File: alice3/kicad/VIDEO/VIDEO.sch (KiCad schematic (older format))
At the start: 4 parts, among them SW1 SW_PUSH, U1 Propeller_P8X32A-D40, Y1 5 MHz

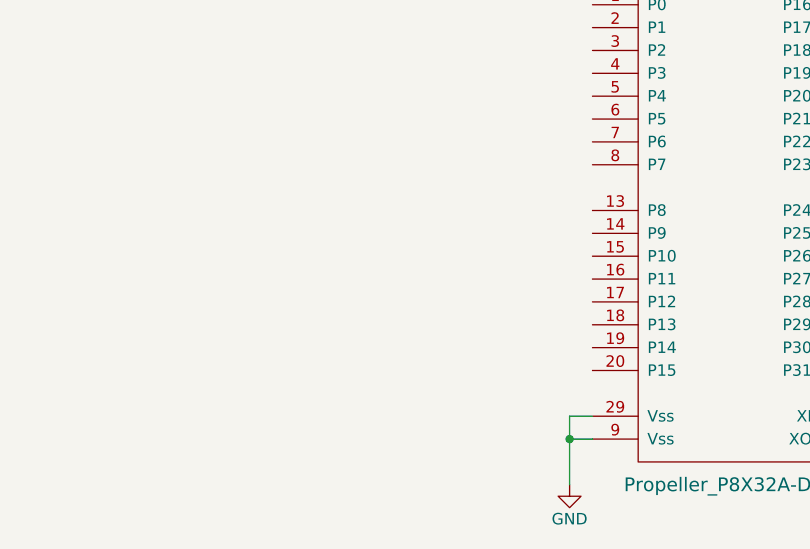
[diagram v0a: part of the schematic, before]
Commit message: Add VGA daughter board.
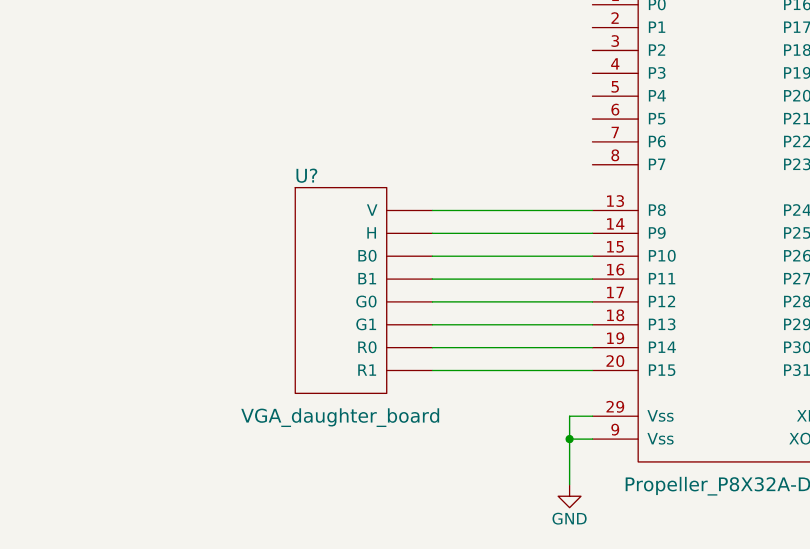
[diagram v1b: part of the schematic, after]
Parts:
- added U?: VGA_daughter_board, symbol VGA_daughter_board
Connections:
- net at U1.13 (P8): now also U?.~ (V)
- net at U1.14 (P9): now also U?.~ (V)
- net at U1.15 (P10): now also U?.~ (V)
- net at U1.16 (P11): now also U?.~ (V)
- net at U1.17 (P12): now also U?.~ (V)
- net at U1.18 (P13): now also U?.~ (V)
- net at U1.19 (P14): now also U?.~ (V)
- net at U1.20 (P15): now also U?.~ (V)
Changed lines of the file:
@@
 LIBS:valves
 LIBS:propeller_p8x32a-d40
+LIBS:vga_daughter_board
 LIBS:VIDEO-cache
 EELAYER 25 0
@@
 Wire Wire Line
 	1000 1200 1000 1500
+$Comp
+L VGA_daughter_board U?
+U 1 1 5681E1A9
+P 3800 3950
+F 0 "U?" H 3550 4450 60  0000 C CNN
+F 1 "VGA_daughter_board" H 3700 3400 60  0000 C CNN
+F 2 "" H 3800 4000 60  0000 C CNN
+F 3 "" H 3800 4000 60  0000 C CNN
+	1    3800 3950
+	1    0    0    -1
+$EndComp
+Wire Wire Line
+	4100 3600 4800 3600
+Wire Wire Line
+	4100 3700 4800 3700
+Wire Wire Line
+	4100 3800 4800 3800
+Wire Wire Line
+	4100 3900 4800 3900
+Wire Wire Line
+	4100 4000 4800 4000
+Wire Wire Line
+	4100 4100 4800 4100
+Wire Wire Line
+	4100 4200 4800 4200
+Wire Wire Line
+	4100 4300 4800 4300
 $EndSCHEMATC

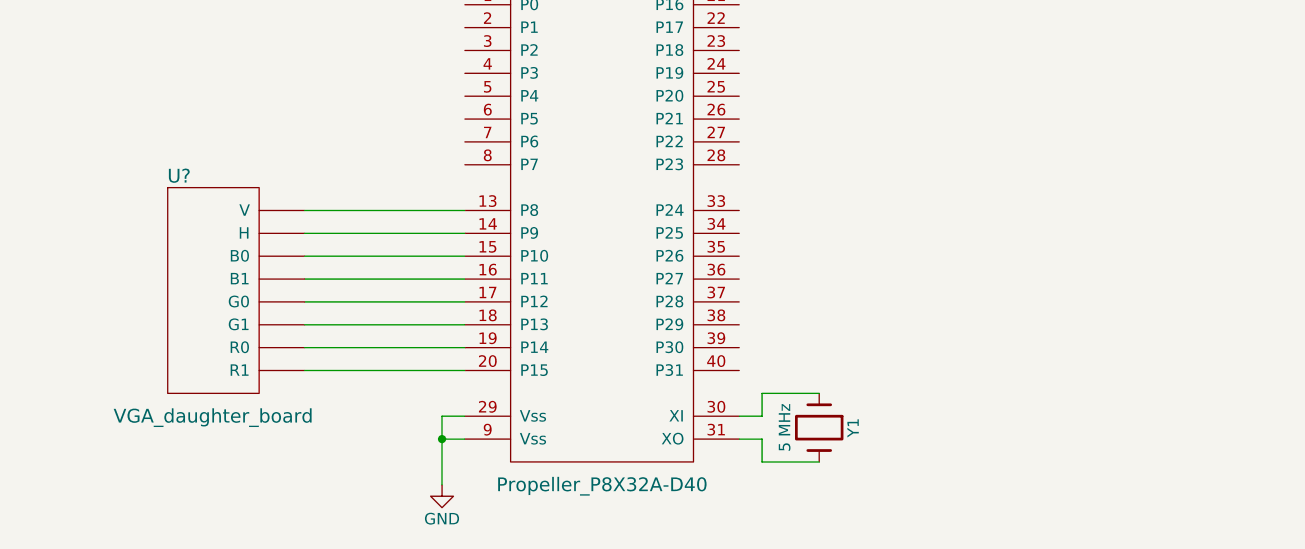
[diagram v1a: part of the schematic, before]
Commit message: Add 24LC256 EEPROM chip to VIDEO board.
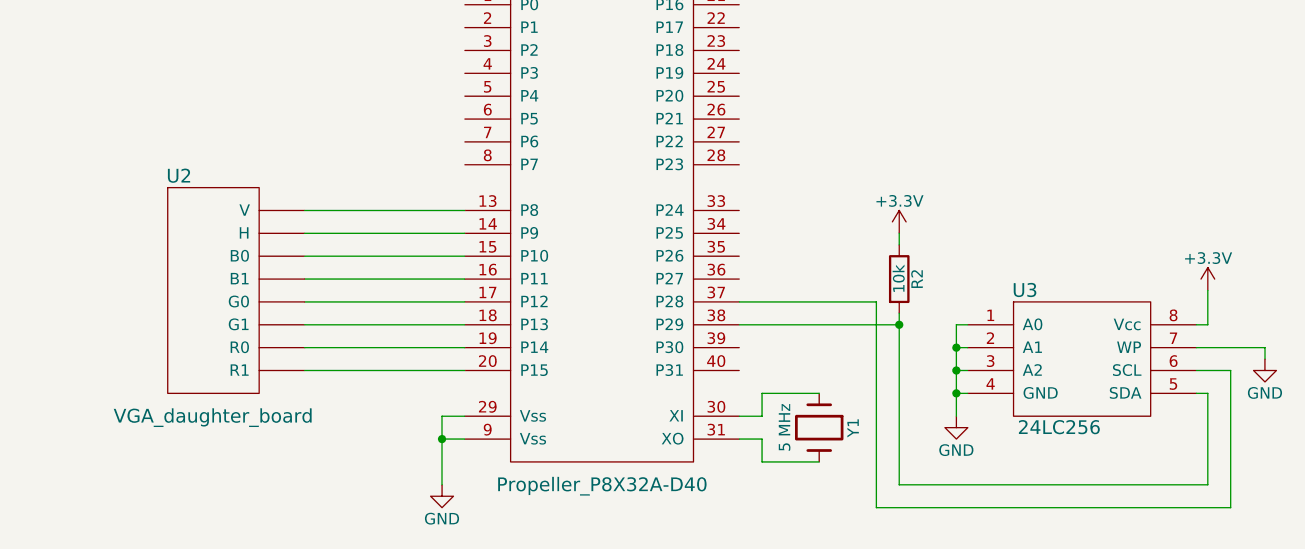
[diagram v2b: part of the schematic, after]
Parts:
- added R2: 10k, symbol R
- added U3: 24LC256, symbol 24LC256
- gave numbers to parts that had none: 1
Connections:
- net +3V3: now also R2.1, U3.8 (Vcc)
- net GND: now also U3.1 (A0), U3.2 (A1), U3.3 (A2), U3.4 (GND), U3.7 (WP)
- net at U1.37 (P28): now also U3.6 (SCL)
- net at U1.38 (P29): now also R2.2, U3.5 (SDA)
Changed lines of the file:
@@
 LIBS:propeller_p8x32a-d40
 LIBS:vga_daughter_board
+LIBS:24lc256
 LIBS:VIDEO-cache
 EELAYER 25 0
@@
 $EndComp
 $Comp
-L GND #PWR01
+L GND #PWR4
 U 1 1 566E4A0D
 P 4700 4800
-F 0 "#PWR01" H 4700 4550 50  0001 C CNN
+F 0 "#PWR4" H 4700 4550 50  0001 C CNN
 F 1 "GND" H 4700 4650 50  0000 C CNN
 F 2 "" H 4700 4800 50  0000 C CNN
@@
 Connection ~ 4700 4600
 $Comp
-L +3.3V #PWR02
+L +3.3V #PWR3
 U 1 1 566E4A37
 P 4700 2200
-F 0 "#PWR02" H 4700 2050 50  0001 C CNN
+F 0 "#PWR3" H 4700 2050 50  0001 C CNN
 F 1 "+3.3V" H 4700 2340 50  0000 C CNN
 F 2 "" H 4700 2200 50  0000 C CNN
@@
 	6100 4700 6350 4700
 $Comp
-L GND #PWR03
+L GND #PWR5
 U 1 1 566E4B37
 P 6300 2500
-F 0 "#PWR03" H 6300 2250 50  0001 C CNN
+F 0 "#PWR5" H 6300 2250 50  0001 C CNN
 F 1 "GND" H 6300 2350 50  0000 C CNN
 F 2 "" H 6300 2500 50  0000 C CNN
@@
 	6000 2500 6300 2500
 $Comp
-L +3.3V #PWR04
+L +3.3V #PWR6
 U 1 1 566E4B67
 P 6500 1800
-F 0 "#PWR04" H 6500 1650 50  0001 C CNN
+F 0 "#PWR6" H 6500 1650 50  0001 C CNN
 F 1 "+3.3V" H 6500 1940 50  0000 C CNN
 F 2 "" H 6500 1800 50  0000 C CNN
@@
 $EndComp
 $Comp
-L GND #PWR05
+L GND #PWR9
 U 1 1 566E4C07
 P 7200 2500
-F 0 "#PWR05" H 7200 2250 50  0001 C CNN
+F 0 "#PWR9" H 7200 2250 50  0001 C CNN
 F 1 "GND" H 7200 2350 50  0000 C CNN
 F 2 "" H 7200 2500 50  0000 C CNN
@@
 	7200 2400 7200 2500
 $Comp
-L PWR_FLAG #FLG06
+L PWR_FLAG #FLG1
 U 1 1 566E4C94
 P 1000 1200
-F 0 "#FLG06" H 1000 1295 50  0001 C CNN
+F 0 "#FLG1" H 1000 1295 50  0001 C CNN
 F 1 "PWR_FLAG" H 1000 1380 50  0000 C CNN
 F 2 "" H 1000 1200 50  0000 C CNN
@@
 $EndComp
 $Comp
-L PWR_FLAG #FLG07
+L PWR_FLAG #FLG2
 U 1 1 566E4CCE
 P 1500 1200
-F 0 "#FLG07" H 1500 1295 50  0001 C CNN
+F 0 "#FLG2" H 1500 1295 50  0001 C CNN
 F 1 "PWR_FLAG" H 1500 1380 50  0000 C CNN
 F 2 "" H 1500 1200 50  0000 C CNN
@@
 $EndComp
 $Comp
-L +3.3V #PWR08
+L +3.3V #PWR1
 U 1 1 566E4D29
 P 1000 1500
-F 0 "#PWR08" H 1000 1350 50  0001 C CNN
+F 0 "#PWR1" H 1000 1350 50  0001 C CNN
 F 1 "+3.3V" H 1000 1640 50  0000 C CNN
 F 2 "" H 1000 1500 50  0000 C CNN
@@
 $EndComp
 $Comp
-L GND #PWR09
+L GND #PWR2
 U 1 1 566E4D40
 P 1500 1500
-F 0 "#PWR09" H 1500 1250 50  0001 C CNN
+F 0 "#PWR2" H 1500 1250 50  0001 C CNN
 F 1 "GND" H 1500 1350 50  0000 C CNN
 F 2 "" H 1500 1500 50  0000 C CNN
@@
 	1000 1200 1000 1500
 $Comp
-L VGA_daughter_board U?
+L VGA_daughter_board U2
 U 1 1 5681E1A9
 P 3800 3950
-F 0 "U?" H 3550 4450 60  0000 C CNN
+F 0 "U2" H 3550 4450 60  0000 C CNN
 F 1 "VGA_daughter_board" H 3700 3400 60  0000 C CNN
 F 2 "" H 3800 4000 60  0000 C CNN
@@
 Wire Wire Line
 	4100 4300 4800 4300
+$Comp
+L 24LC256 U3
+U 1 1 5681F117
+P 7500 4250
+F 0 "U3" H 7250 4550 60  0000 C CNN
+F 1 "24LC256" H 7400 3950 60  0000 C CNN
+F 2 "" H 7500 4150 60  0000 C CNN
+F 3 "" H 7500 4150 60  0000 C CNN
+	1    7500 4250
+	1    0    0    -1
+$EndComp
+$Comp
+L GND #PWR8
+U 1 1 5681F164
+P 6950 4500
+F 0 "#PWR8" H 6950 4250 50  0001 C CNN
+F 1 "GND" H 6950 4350 50  0000 C CNN
+F 2 "" H 6950 4500 50  0000 C CNN
+F 3 "" H 6950 4500 50  0000 C CNN
+	1    6950 4500
+	1    0    0    -1
+$EndComp
+Wire Wire Line
+	7000 4100 6950 4100
+Wire Wire Line
+	6950 4100 6950 4500
+Wire Wire Line
+	7000 4200 6950 4200
+Connection ~ 6950 4200
+Wire Wire Line
+	7000 4300 6950 4300
+Connection ~ 6950 4300
+Wire Wire Line
+	7000 4400 6950 4400
+Connection ~ 6950 4400
+$Comp
+L +3.3V #PWR10
+U 1 1 5681F2C2
+P 8050 3950
+F 0 "#PWR10" H 8050 3800 50  0001 C CNN
+F 1 "+3.3V" H 8050 4090 50  0000 C CNN
+F 2 "" H 8050 3950 50  0000 C CNN
+F 3 "" H 8050 3950 50  0000 C CNN
+	1    8050 3950
+	1    0    0    -1
+$EndComp
+$Comp
+L GND #PWR11
+U 1 1 5681F2E8
+P 8300 4250
+F 0 "#PWR11" H 8300 4000 50  0001 C CNN
+F 1 "GND" H 8300 4100 50  0000 C CNN
+F 2 "" H 8300 4250 50  0000 C CNN
+F 3 "" H 8300 4250 50  0000 C CNN
+	1    8300 4250
+	1    0    0    -1
+$EndComp
+Wire Wire Line
+	8000 4100 8050 4100
+Wire Wire Line
+	8050 4100 8050 3950
+Wire Wire Line
+	8000 4200 8300 4200
+Wire Wire Line
+	8300 4200 8300 4250
+Wire Wire Line
+	8000 4300 8150 4300
+Wire Wire Line
+	8150 4300 8150 4900
+Wire Wire Line
+	8150 4900 6600 4900
+Wire Wire Line
+	6600 4900 6600 4000
+Wire Wire Line
+	6600 4000 6000 4000
+Wire Wire Line
+	8000 4400 8050 4400
+Wire Wire Line
+	8050 4400 8050 4800
+Wire Wire Line
+	8050 4800 6700 4800
+Wire Wire Line
+	6700 4800 6700 4050
+Wire Wire Line
+	6700 4100 6000 4100
+$Comp
+L +3.3V #PWR7
+U 1 1 5681F435
+P 6700 3700
+F 0 "#PWR7" H 6700 3550 50  0001 C CNN
+F 1 "+3.3V" H 6700 3840 50  0000 C CNN
+F 2 "" H 6700 3700 50  0000 C CNN
+F 3 "" H 6700 3700 50  0000 C CNN
+	1    6700 3700
+	1    0    0    -1
+$EndComp
+$Comp
+L R R2
+U 1 1 5681F454
+P 6700 3900
+F 0 "R2" V 6780 3900 50  0000 C CNN
+F 1 "10k" V 6700 3900 50  0000 C CNN
+F 2 "" V 6630 3900 50  0000 C CNN
+F 3 "" H 6700 3900 50  0000 C CNN
+	1    6700 3900
+	1    0    0    -1
+$EndComp
+Connection ~ 6700 4100
+Wire Wire Line
+	6700 3750 6700 3700
 $EndSCHEMATC

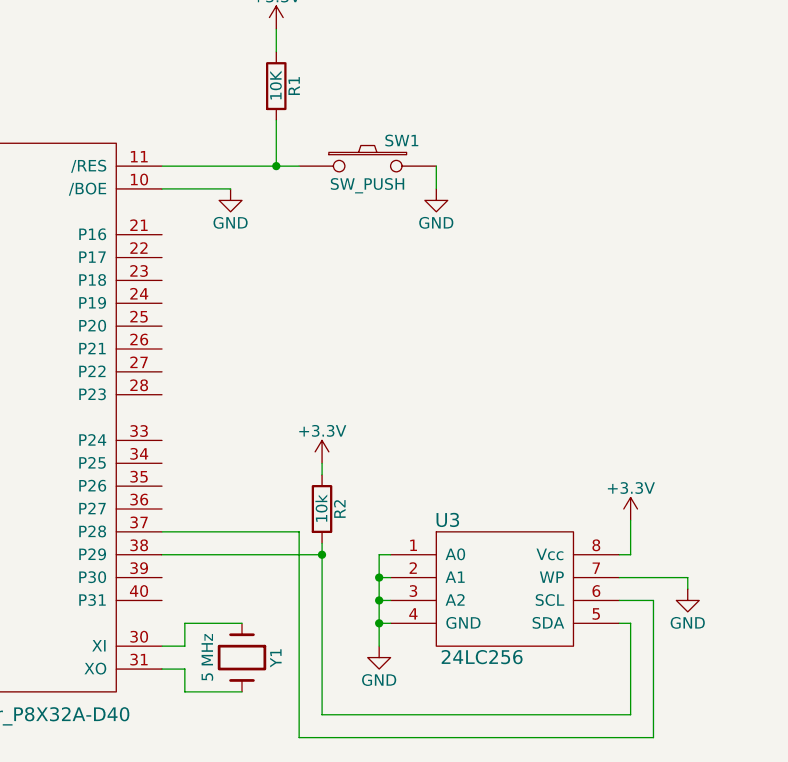
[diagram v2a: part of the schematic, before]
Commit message: Add Propeller Plug (USB programmer).
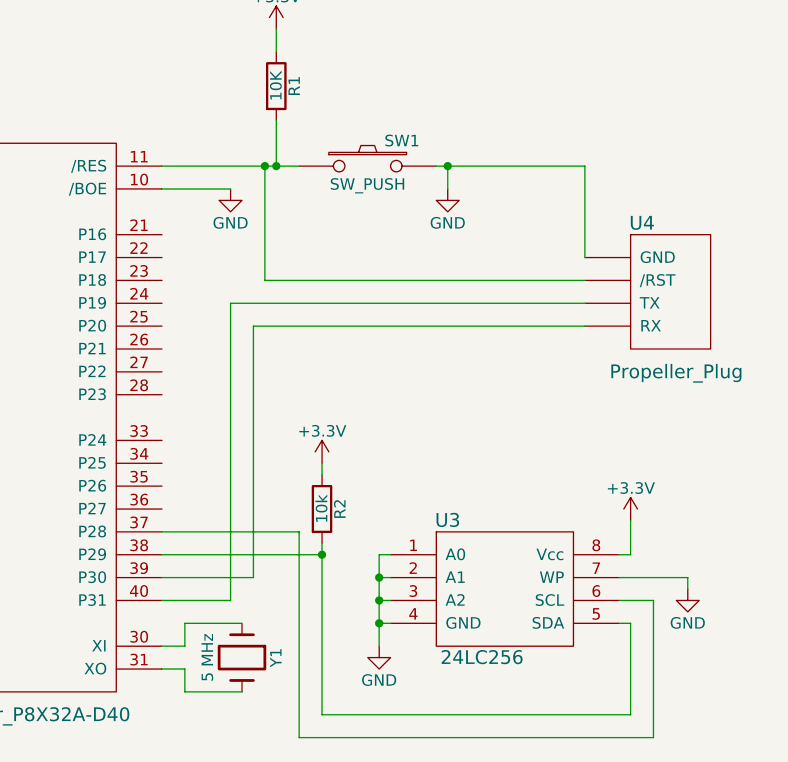
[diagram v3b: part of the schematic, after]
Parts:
- added U4: Propeller_Plug, symbol Propeller_Plug
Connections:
- net GND: now also U4.~ (TX)
- net at R1.2, SW1.1, U1.11 (/RES): now also U4.~ (TX)
- net at U1.39 (P30): now also U4.~ (TX)
- net at U1.40 (P31): now also U4.~ (TX)
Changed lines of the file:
@@
 LIBS:vga_daughter_board
 LIBS:24lc256
+LIBS:propeller_plug
 LIBS:VIDEO-cache
 EELAYER 25 0
@@
 	1    0    0    -1
 $EndComp
-Wire Wire Line
-	4800 4500 4700 4500
-Wire Wire Line
-	4700 4500 4700 4800
-Wire Wire Line
-	4800 4600 4700 4600
-Connection ~ 4700 4600
 $Comp
 L +3.3V #PWR3
@@
 	1    0    0    -1
 $EndComp
-Wire Wire Line
-	4700 2500 4800 2500
-Wire Wire Line
-	4700 2200 4700 2500
-Wire Wire Line
-	4800 2400 4700 2400
-Connection ~ 4700 2400
 $Comp
 L Crystal Y1
@@
 	0    1    1    0
 $EndComp
-Wire Wire Line
-	6000 4500 6100 4500
-Wire Wire Line
-	6100 4500 6100 4400
-Wire Wire Line
-	6100 4400 6350 4400
-Wire Wire Line
-	6000 4600 6100 4600
-Wire Wire Line
-	6100 4600 6100 4700
-Wire Wire Line
-	6100 4700 6350 4700
 $Comp
 L GND #PWR5
@@
 	1    0    0    -1
 $EndComp
-Wire Wire Line
-	6000 2500 6300 2500
 $Comp
 L +3.3V #PWR6
@@
 L GND #PWR9
 U 1 1 566E4C07
-P 7200 2500
-F 0 "#PWR9" H 7200 2250 50  0001 C CNN
-F 1 "GND" H 7200 2350 50  0000 C CNN
-F 2 "" H 7200 2500 50  0000 C CNN
-F 3 "" H 7200 2500 50  0000 C CNN
-	1    7200 2500
-	1    0    0    -1
-$EndComp
-Wire Wire Line
-	6500 1900 6500 1800
-Wire Wire Line
-	6000 2400 6600 2400
-Wire Wire Line
-	6500 2400 6500 2200
-Connection ~ 6500 2400
-Wire Wire Line
-	7200 2400 7200 2500
+P 7250 2500
+F 0 "#PWR9" H 7250 2250 50  0001 C CNN
+F 1 "GND" H 7250 2350 50  0000 C CNN
+F 2 "" H 7250 2500 50  0000 C CNN
+F 3 "" H 7250 2500 50  0000 C CNN
+	1    7250 2500
+	1    0    0    -1
+$EndComp
 $Comp
 L PWR_FLAG #FLG1
@@
 	1    0    0    -1
 $EndComp
-Wire Wire Line
-	1500 1200 1500 1500
-Wire Wire Line
-	1000 1200 1000 1500
 $Comp
 L VGA_daughter_board U2
@@
 	1    0    0    -1
 $EndComp
-Wire Wire Line
-	4100 3600 4800 3600
-Wire Wire Line
-	4100 3700 4800 3700
-Wire Wire Line
-	4100 3800 4800 3800
-Wire Wire Line
-	4100 3900 4800 3900
-Wire Wire Line
-	4100 4000 4800 4000
-Wire Wire Line
-	4100 4100 4800 4100
-Wire Wire Line
-	4100 4200 4800 4200
-Wire Wire Line
-	4100 4300 4800 4300
 $Comp
 L 24LC256 U3
@@
 	1    0    0    -1
 $EndComp
-Wire Wire Line
-	7000 4100 6950 4100
-Wire Wire Line
-	6950 4100 6950 4500
-Wire Wire Line
-	7000 4200 6950 4200
-Connection ~ 6950 4200
-Wire Wire Line
-	7000 4300 6950 4300
-Connection ~ 6950 4300
-Wire Wire Line
-	7000 4400 6950 4400
-Connection ~ 6950 4400
 $Comp
 L +3.3V #PWR10
@@
 	1    0    0    -1
 $EndComp
-Wire Wire Line
-	8000 4100 8050 4100
-Wire Wire Line
-	8050 4100 8050 3950
-Wire Wire Line
-	8000 4200 8300 4200
-Wire Wire Line
-	8300 4200 8300 4250
-Wire Wire Line
-	8000 4300 8150 4300
-Wire Wire Line
-	8150 4300 8150 4900
-Wire Wire Line
-	8150 4900 6600 4900
-Wire Wire Line
-	6600 4900 6600 4000
-Wire Wire Line
-	6600 4000 6000 4000
-Wire Wire Line
-	8000 4400 8050 4400
-Wire Wire Line
-	8050 4400 8050 4800
-Wire Wire Line
-	8050 4800 6700 4800
-Wire Wire Line
-	6700 4800 6700 4050
-Wire Wire Line
-	6700 4100 6000 4100
 $Comp
 L +3.3V #PWR7
@@
 	1    0    0    -1
 $EndComp
+$Comp
+L Propeller_Plug U4
+U 1 1 5681F4AC
+P 8200 2950
+F 0 "U4" H 8100 3250 60  0000 C CNN
+F 1 "Propeller_Plug" H 8250 2600 60  0000 C CNN
+F 2 "" H 8200 2950 60  0000 C CNN
+F 3 "" H 8200 2950 60  0000 C CNN
+	1    8200 2950
+	1    0    0    -1
+$EndComp
+Wire Wire Line
+	4800 4500 4700 4500
+Wire Wire Line
+	4700 4500 4700 4800
+Wire Wire Line
+	4800 4600 4700 4600
+Connection ~ 4700 4600
+Wire Wire Line
+	4700 2500 4800 2500
+Wire Wire Line
+	4700 2200 4700 2500
+Wire Wire Line
+	4800 2400 4700 2400
+Connection ~ 4700 2400
+Wire Wire Line
+	6000 4500 6100 4500
+Wire Wire Line
+	6100 4500 6100 4400
+Wire Wire Line
+	6100 4400 6350 4400
+Wire Wire Line
+	6000 4600 6100 4600
+Wire Wire Line
+	6100 4600 6100 4700
+Wire Wire Line
+	6100 4700 6350 4700
+Wire Wire Line
+	6000 2500 6300 2500
+Wire Wire Line
+	6500 1900 6500 1800
+Wire Wire Line
+	6000 2400 6600 2400
+Wire Wire Line
+	6500 2400 6500 2200
+Connection ~ 6500 2400
+Wire Wire Line
+	1500 1200 1500 1500
+Wire Wire Line
+	1000 1200 1000 1500
+Wire Wire Line
+	4100 3600 4800 3600
+Wire Wire Line
+	4100 3700 4800 3700
+Wire Wire Line
+	4100 3800 4800 3800
+Wire Wire Line
+	4100 3900 4800 3900
+Wire Wire Line
+	4100 4000 4800 4000
+Wire Wire Line
+	4100 4100 4800 4100
+Wire Wire Line
+	4100 4200 4800 4200
+Wire Wire Line
+	4100 4300 4800 4300
+Wire Wire Line
+	7000 4100 6950 4100
+Wire Wire Line
+	6950 4100 6950 4500
+Wire Wire Line
+	7000 4200 6950 4200
+Connection ~ 6950 4200
+Wire Wire Line
+	7000 4300 6950 4300
+Connection ~ 6950 4300
+Wire Wire Line
+	7000 4400 6950 4400
+Connection ~ 6950 4400
+Wire Wire Line
+	8000 4100 8050 4100
+Wire Wire Line
+	8050 4100 8050 3950
+Wire Wire Line
+	8000 4200 8300 4200
+Wire Wire Line
+	8300 4200 8300 4250
+Wire Wire Line
+	8000 4300 8150 4300
+Wire Wire Line
+	8150 4300 8150 4900
+Wire Wire Line
+	8150 4900 6600 4900
+Wire Wire Line
+	6600 4900 6600 4000
+Wire Wire Line
+	6600 4000 6000 4000
+Wire Wire Line
+	8000 4400 8050 4400
+Wire Wire Line
+	8050 4400 8050 4800
+Wire Wire Line
+	8050 4800 6700 4800
+Wire Wire Line
+	6700 4800 6700 4050
+Wire Wire Line
+	6700 4100 6000 4100
 Connection ~ 6700 4100
 Wire Wire Line
 	6700 3750 6700 3700
+Wire Wire Line
+	7850 2900 6450 2900
+Wire Wire Line
+	6450 2900 6450 2400
+Connection ~ 6450 2400
+Wire Wire Line
+	7850 3000 6300 3000
+Wire Wire Line
+	6300 3000 6300 4300
+Wire Wire Line
+	6300 4300 6000 4300
+Wire Wire Line
+	7850 3100 6400 3100
+Wire Wire Line
+	6400 3100 6400 4200
+Wire Wire Line
+	6400 4200 6000 4200
+Wire Wire Line
+	7850 2400 7850 2800
+Wire Wire Line
+	7200 2400 7850 2400
+Wire Wire Line
+	7250 2400 7250 2500
+Connection ~ 7250 2400
 $EndSCHEMATC
